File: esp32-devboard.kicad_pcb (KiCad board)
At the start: 2 copper layers, 1 part, among them U1 ESP32-C6-MINI-1/U

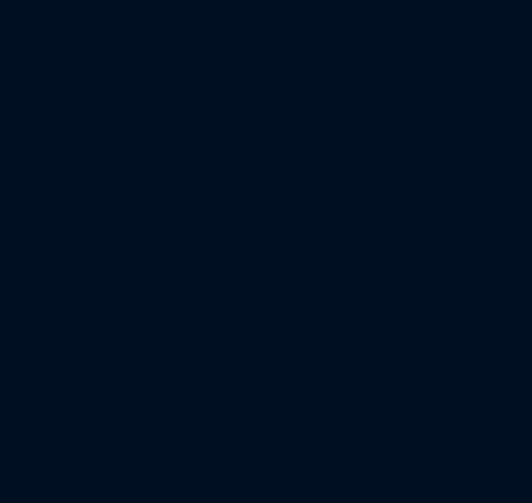
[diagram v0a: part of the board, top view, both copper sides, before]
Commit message: added USB-C connector
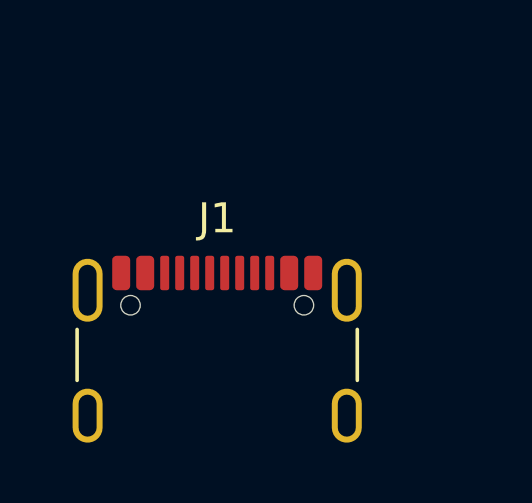
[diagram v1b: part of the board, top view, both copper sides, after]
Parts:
- added J1: USB_C_Receptacle_USB2.0_16P, Connector_USB:USB_C_Receptacle_GCT_USB4105-xx-A_16P_TopMnt_Horizontal, F.Cu at (132.7, 143.9)
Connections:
- net Net-(U1-GND-Pad1) renamed GND
- U1 pad 17: unconnected-(U1-GPIO12/USB_D--Pad17) -> /ESP32/USB_D-
- U1 pad 18: unconnected-(U1-GPIO13/USB_D+-Pad18) -> /ESP32/USB_D+
- U1 pad 3: unconnected-(U1-3V3-Pad3) -> +3.3V
- U1 pad 8: unconnected-(U1-EN/CHIP_PU-Pad8) -> /ESP32/ESP32_EN

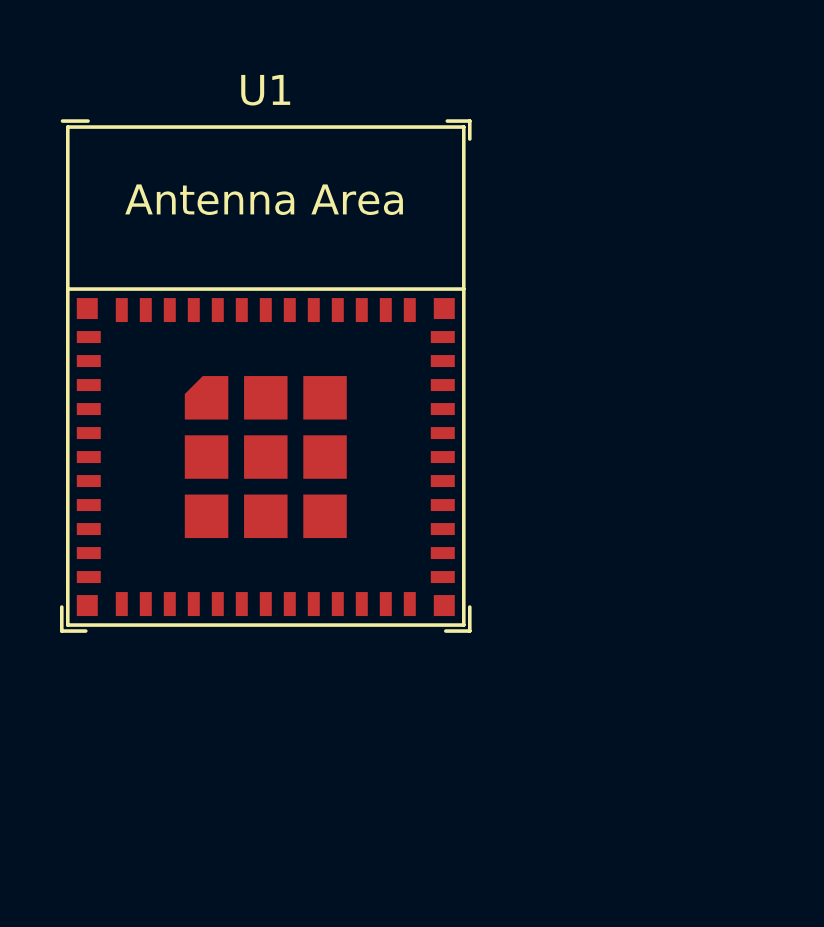
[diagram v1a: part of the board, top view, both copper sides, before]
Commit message: add P/N
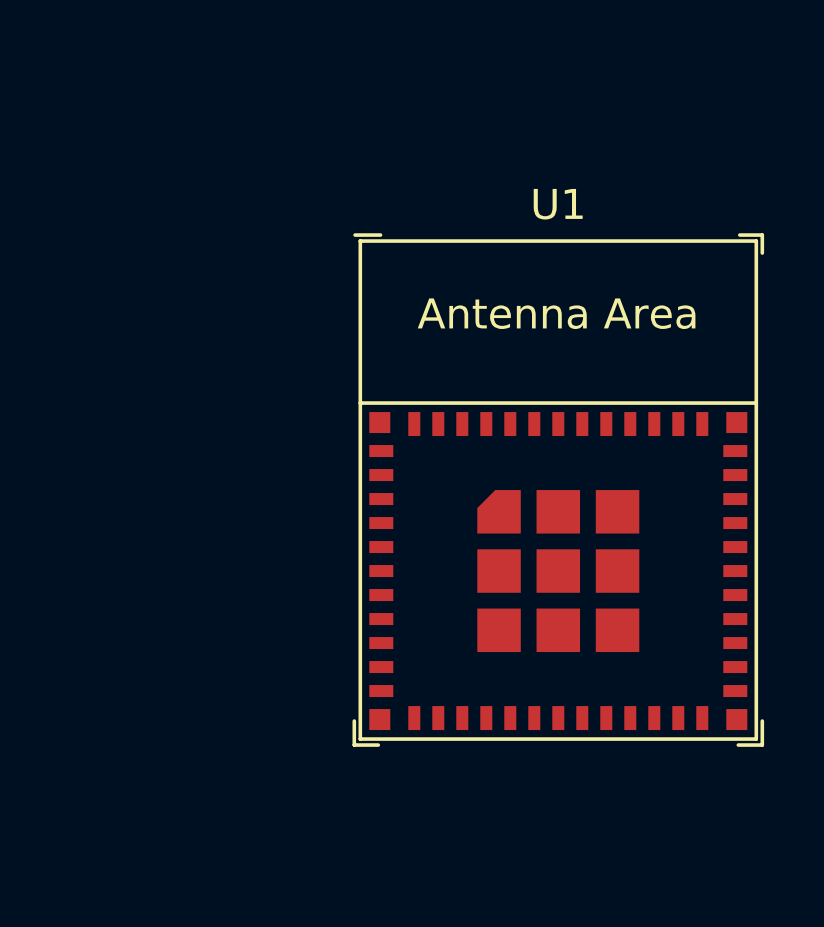
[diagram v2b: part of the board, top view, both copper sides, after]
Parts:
- moved U1 10.5 mm to (144.1, 91.2)
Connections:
- net /ESP32/ESP32_EN renamed /Devices/RST
- net /USB/+5V_USB renamed /USB/VBUSB
- U1 pad 12: unconnected-(U1-GPIO0/ADC1_CH0/XTAL_32K_P-Pad12) -> /ESP32/GPIO_0
- U1 pad 13: unconnected-(U1-GPIO1/ADC1_CH1/XTAL_32K_N-Pad13) -> /ESP32/GPIO_1
- U1 pad 19: unconnected-(U1-GPIO14-Pad19) -> /Devices/FLIP
- U1 pad 20: unconnected-(U1-GPIO15-Pad20) -> /Devices/FLOP
- U1 pad 22: unconnected-(U1-GPIO8-Pad22) -> /ESP32/GPIO_8
- U1 pad 23: unconnected-(U1-GPIO9-Pad23) -> /Devices/BOOT
- U1 pad 24: unconnected-(U1-GPIO18-Pad24) -> /Devices/LED_0
- U1 pad 27: unconnected-(U1-GPIO21-Pad27) -> /ESP32/GPIO_21
- U1 pad 28: unconnected-(U1-GPIO22-Pad28) -> /ESP32/GPIO_22
- U1 pad 29: unconnected-(U1-GPIO23-Pad29) -> /ESP32/GPIO_23
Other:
- copper layers 2 -> 4
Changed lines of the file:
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@@
 	(layers
 		(0 "F.Cu" signal)
+		(1 "In1.Cu" signal)
+		(2 "In2.Cu" signal)
 		(31 "B.Cu" signal)
 		(32 "B.Adhes" user "B.Adhesive")
@@
 	)
 	(setup
+		(stackup
+			(layer "F.SilkS"
+				(type "Top Silk Screen")
+			)
+			(layer "F.Paste"
+				(type "Top Solder Paste")
+			)
+			(layer "F.Mask"
+				(type "Top Solder Mask")
+				(thickness 0.01)
+			)
+			(layer "F.Cu"
+				(type "copper")
+				(thickness 0.035)
+			)
+			(layer "dielectric 1"
+				(type "core")
+				(thickness 0.1)
+				(material "FR4")
+				(epsilon_r 4.5)
+				(loss_tangent 0.02)
+			)
+			(layer "In1.Cu"
+				(type "copper")
+				(thickness 0.035)
+			)
+			(layer "dielectric 2"
+				(type "core")
+				(thickness 1.24)
+				(material "FR4")
+				(epsilon_r 4.5)
+				(loss_tangent 0.02)
+			)
+			(layer "In2.Cu"
+				(type "copper")
+				(thickness 0.035)
+			)
+			(layer "dielectric 3"
+				(type "prepreg")
+				(thickness 0.1)
+				(material "FR4")
+				(epsilon_r 4.5)
+				(loss_tangent 0.02)
+			)
+			(layer "B.Cu"
+				(type "copper")
+				(thickness 0.035)
+			)
+			(layer "B.Mask"
+				(type "Bottom Solder Mask")
+				(thickness 0.01)
+			)
+			(layer "B.Paste"
+				(type "Bottom Solder Paste")
+			)
+			(layer "B.SilkS"
+				(type "Bottom Silk Screen")
+			)
+			(copper_finish "None")
+			(dielectric_constraints no)
+		)
 		(pad_to_mask_clearance 0)
 		(allow_soldermask_bridges_in_footprints no)
@@
 	(net 4 "unconnected-(U1-NC-Pad32)")
 	(net 5 "unconnected-(U1-NC-Pad4)")
-	(net 6 "unconnected-(U1-GPIO1{slash}ADC1_CH1{slash}XTAL_32K_N-Pad13)")
+	(net 6 "/USB/VBUSB")
 	(net 7 "unconnected-(U1-MTDI{slash}GPIO5{slash}ADC1_CH5-Pad10)")
 	(net 8 "unconnected-(U1-U0RXD{slash}GPIO17-Pad30)")
@@
 	(net 11 "unconnected-(U1-MTCK{slash}GPIO6{slash}ADC1_CH6-Pad15)")
 	(net 12 "unconnected-(U1-U0TXD{slash}GPIO16-Pad31)")
-	(net 13 "unconnected-(U1-GPIO18-Pad24)")
+	(net 13 "/ESP32/GPIO_1")
 	(net 14 "unconnected-(U1-MTDO{slash}GPIO7-Pad16)")
-	(net 15 "unconnected-(U1-GPIO8-Pad22)")
+	(net 15 "/Devices/LED_0")
 	(net 16 "unconnected-(U1-NC-Pad35)")
-	(net 17 "unconnected-(U1-GPIO0{slash}ADC1_CH0{slash}XTAL_32K_P-Pad12)")
-	(net 18 "unconnected-(U1-GPIO14-Pad19)")
-	(net 19 "unconnected-(U1-GPIO21-Pad27)")
-	(net 20 "unconnected-(U1-GPIO9-Pad23)")
+	(net 17 "/ESP32/GPIO_8")
+	(net 18 "/ESP32/GPIO_0")
+	(net 19 "/Devices/FLIP")
+	(net 20 "/ESP32/GPIO_21")
 	(net 21 "unconnected-(U1-GPIO19-Pad25)")
 	(net 22 "unconnected-(U1-NC-Pad34)")
 	(net 23 "unconnected-(U1-MTMS{slash}GPIO4{slash}ADC1_CH4-Pad9)")
-	(net 24 "unconnected-(U1-GPIO15-Pad20)")
-	(net 25 "unconnected-(U1-GPIO22-Pad28)")
+	(net 24 "/Devices/BOOT")
+	(net 25 "/Devices/FLOP")
 	(net 26 "unconnected-(U1-NC-Pad33)")
-	(net 27 "unconnected-(U1-GPIO23-Pad29)")
+	(net 27 "/Devices/RST")
 	(net 28 "GND")
 	(net 29 "+3.3V")
-	(net 30 "/ESP32/ESP32_EN")
+	(net 30 "/ESP32/GPIO_22")
 	(net 31 "/ESP32/USB_D-")
 	(net 32 "/ESP32/USB_D+")
 	(net 33 "/USB/CC2")
-	(net 34 "/USB/+5V_USB")
+	(net 34 "/ESP32/GPIO_23")
 	(net 35 "unconnected-(J1-SBU1-PadA8)")
 	(net 36 "/USB/CC1")
@@
 			)
 		)
-		(property "Datasheet" "https://www.usb.org/sites/default/files/documents/usb_type-c.zip"
+		(property "Datasheet" "https://www.mouser.com/datasheet/2/837/usb4215-3472997.pdf"
 			(at 0 0 0)
 			(unlocked yes)
@@
 				(font
 					(size 1.27 1.27)
+					(thickness 0.15)
+				)
+			)
+		)
+		(property "P/N" "640-USB4215-03-A"
+			(at 0 0 0)
+			(unlocked yes)
+			(layer "F.Fab")
+			(hide yes)
+			(effects
+				(font
+					(size 1 1)
 					(thickness 0.15)
 				)
@@
 			(layers "F.Cu" "F.Paste" "F.Mask")
 			(roundrect_rratio 0.25)
-			(net 34 "/USB/+5V_USB")
+			(net 6 "/USB/VBUSB")
 			(pinfunction "VBUS")
 			(pintype "passive")
@@
 			(layers "F.Cu" "F.Paste" "F.Mask")
 			(roundrect_rratio 0.25)
-			(net 34 "/USB/+5V_USB")
+			(net 6 "/USB/VBUSB")
 			(pinfunction "VBUS")
 			(pintype "passive")
@@
 			(layers "F.Cu" "F.Paste" "F.Mask")
 			(roundrect_rratio 0.25)
-			(net 34 "/USB/+5V_USB")
+			(net 6 "/USB/VBUSB")
 			(pinfunction "VBUS")
 			(pintype "passive")
@@
 			(layers "F.Cu" "F.Paste" "F.Mask")
 			(roundrect_rratio 0.25)
-			(net 34 "/USB/+5V_USB")
+			(net 6 "/USB/VBUSB")
 			(pinfunction "VBUS")
 			(pintype "passive")
@@
 	(footprint "PCM_Espressif:ESP32-C6-MINI-1"
 		(layer "F.Cu")
-		(at 134.3 87.35)
+		(at 144.05 91.15)
 		(descr "ESP32-C6-MINI-1: https://www.espressif.com/sites/default/files/documentation/esp32-c6-mini-1_datasheet_en.pdf")
 		(tags "ESP32-C6")
@@
 			(net 10 "unconnected-(U1-GPIO2{slash}ADC1_CH2-Pad5)")
 			(pinfunction "GPIO2/ADC1_CH2")
-			(pintype "bidirectional")
+			(pintype "bidirectional+no_connect")
 		)
 		(pad "6" smd rect
@@
 			(net 1 "unconnected-(U1-GPIO3{slash}ADC1_CH3-Pad6)")
 			(pinfunction "GPIO3/ADC1_CH3")
-			(pintype "bidirectional")
+			(pintype "bidirectional+no_connect")
 		)
 		(pad "7" smd rect
@@
 			(size 0.4 0.8)
 			(layers "F.Cu" "F.Paste" "F.Mask")
-			(net 30 "/ESP32/ESP32_EN")
+			(net 27 "/Devices/RST")
 			(pinfunction "EN/CHIP_PU")
 			(pintype "input")
@@
 			(net 23 "unconnected-(U1-MTMS{slash}GPIO4{slash}ADC1_CH4-Pad9)")
 			(pinfunction "MTMS/GPIO4/ADC1_CH4")
-			(pintype "bidirectional")
+			(pintype "bidirectional+no_connect")
 		)
 		(pad "10" smd rect
@@
 			(net 7 "unconnected-(U1-MTDI{slash}GPIO5{slash}ADC1_CH5-Pad10)")
 			(pinfunction "MTDI/GPIO5/ADC1_CH5")
-			(pintype "bidirectional")
+			(pintype "bidirectional+no_connect")
 		)
 		(pad "11" smd rect
@@
 			(size 0.4 0.8)
 			(layers "F.Cu" "F.Paste" "F.Mask")
-			(net 17 "unconnected-(U1-GPIO0{slash}ADC1_CH0{slash}XTAL_32K_P-Pad12)")
+			(net 18 "/ESP32/GPIO_0")
 			(pinfunction "GPIO0/ADC1_CH0/XTAL_32K_P")
 			(pintype "bidirectional")
@@
 			(size 0.4 0.8)
 			(layers "F.Cu" "F.Paste" "F.Mask")
-			(net 6 "unconnected-(U1-GPIO1{slash}ADC1_CH1{slash}XTAL_32K_N-Pad13)")
+			(net 13 "/ESP32/GPIO_1")
 			(pinfunction "GPIO1/ADC1_CH1/XTAL_32K_N")
 			(pintype "bidirectional")
@@
 			(net 11 "unconnected-(U1-MTCK{slash}GPIO6{slash}ADC1_CH6-Pad15)")
 			(pinfunction "MTCK/GPIO6/ADC1_CH6")
-			(pintype "bidirectional")
+			(pintype "bidirectional+no_connect")
 		)
 		(pad "16" smd rect
@@
 			(net 14 "unconnected-(U1-MTDO{slash}GPIO7-Pad16)")
 			(pinfunction "MTDO/GPIO7")
-			(pintype "bidirectional")
+			(pintype "bidirectional+no_connect")
 		)
 		(pad "17" smd rect
@@
 			(size 0.4 0.8)
 			(layers "F.Cu" "F.Paste" "F.Mask")
-			(net 18 "unconnected-(U1-GPIO14-Pad19)")
+			(net 19 "/Devices/FLIP")
 			(pinfunction "GPIO14")
 			(pintype "bidirectional")
@@
 			(size 0.4 0.8)
 			(layers "F.Cu" "F.Paste" "F.Mask")
-			(net 24 "unconnected-(U1-GPIO15-Pad20)")
+			(net 25 "/Devices/FLOP")
 			(pinfunction "GPIO15")
 			(pintype "bidirectional")
@@
 			(size 0.4 0.8)
 			(layers "F.Cu" "F.Paste" "F.Mask")
-			(net 15 "unconnected-(U1-GPIO8-Pad22)")
+			(net 17 "/ESP32/GPIO_8")
 			(pinfunction "GPIO8")
 			(pintype "bidirectional")
@@
 			(size 0.4 0.8)
 			(layers "F.Cu" "F.Paste" "F.Mask")
-			(net 20 "unconnected-(U1-GPIO9-Pad23)")
+			(net 24 "/Devices/BOOT")
 			(pinfunction "GPIO9")
 			(pintype "bidirectional")
@@
 			(size 0.4 0.8)
 			(layers "F.Cu" "F.Paste" "F.Mask")
-			(net 13 "unconnected-(U1-GPIO18-Pad24)")
+			(net 15 "/Devices/LED_0")
 			(pinfunction "GPIO18")
 			(pintype "bidirectional")
@@
 			(net 21 "unconnected-(U1-GPIO19-Pad25)")
 			(pinfunction "GPIO19")
-			(pintype "bidirectional")
+			(pintype "bidirectional+no_connect")
 		)
 		(pad "26" smd rect
@@
 			(net 9 "unconnected-(U1-GPIO20-Pad26)")
 			(pinfunction "GPIO20")
-			(pintype "bidirectional")
+			(pintype "bidirectional+no_connect")
 		)
 		(pad "27" smd rect
@@
 			(size 0.4 0.8)
 			(layers "F.Cu" "F.Paste" "F.Mask")
-			(net 19 "unconnected-(U1-GPIO21-Pad27)")
+			(net 20 "/ESP32/GPIO_21")
 			(pinfunction "GPIO21")
 			(pintype "bidirectional")
@@
 			(size 0.4 0.8)
 			(layers "F.Cu" "F.Paste" "F.Mask")
-			(net 25 "unconnected-(U1-GPIO22-Pad28)")
+			(net 30 "/ESP32/GPIO_22")
 			(pinfunction "GPIO22")
 			(pintype "bidirectional")
@@
 			(size 0.4 0.8)
 			(layers "F.Cu" "F.Paste" "F.Mask")
-			(net 27 "unconnected-(U1-GPIO23-Pad29)")
+			(net 34 "/ESP32/GPIO_23")
 			(pinfunction "GPIO23")
 			(pintype "bidirectional")
@@
 			(net 8 "unconnected-(U1-U0RXD{slash}GPIO17-Pad30)")
 			(pinfunction "U0RXD/GPIO17")
-			(pintype "bidirectional")
+			(pintype "bidirectional+no_connect")
 		)
 		(pad "31" smd rect
@@
 			(net 12 "unconnected-(U1-U0TXD{slash}GPIO16-Pad31)")
 			(pinfunction "U0TXD/GPIO16")
-			(pintype "bidirectional")
+			(pintype "bidirectional+no_connect")
 		)
 		(pad "32" smd rect
@@
 			(polygon
 				(pts
-					(xy 140.9 84.45) (xy 127.7 84.45) (xy 127.7 79.05) (xy 140.9 79.05)
+					(xy 150.65 88.25) (xy 137.45 88.25) (xy 137.45 82.85) (xy 150.65 82.85)
 				)
 			)
@@
 		(polygon
 			(pts
-				(xy 112.7 84.45) (xy 112.7 64.05) (xy 155.9 64.05) (xy 155.9 84.45)
-			)
-		)
+				(xy 122.45 88.25) (xy 122.45 67.85) (xy 165.65 67.85) (xy 165.65 88.25)
+			)
+		)
+	)
+	(group ""
+		(members "9e491c97-c408-47aa-a825-656574b5255b" "efe0206d-e05d-4263-8e52-4d6ee51e22c0")
 	)
 )

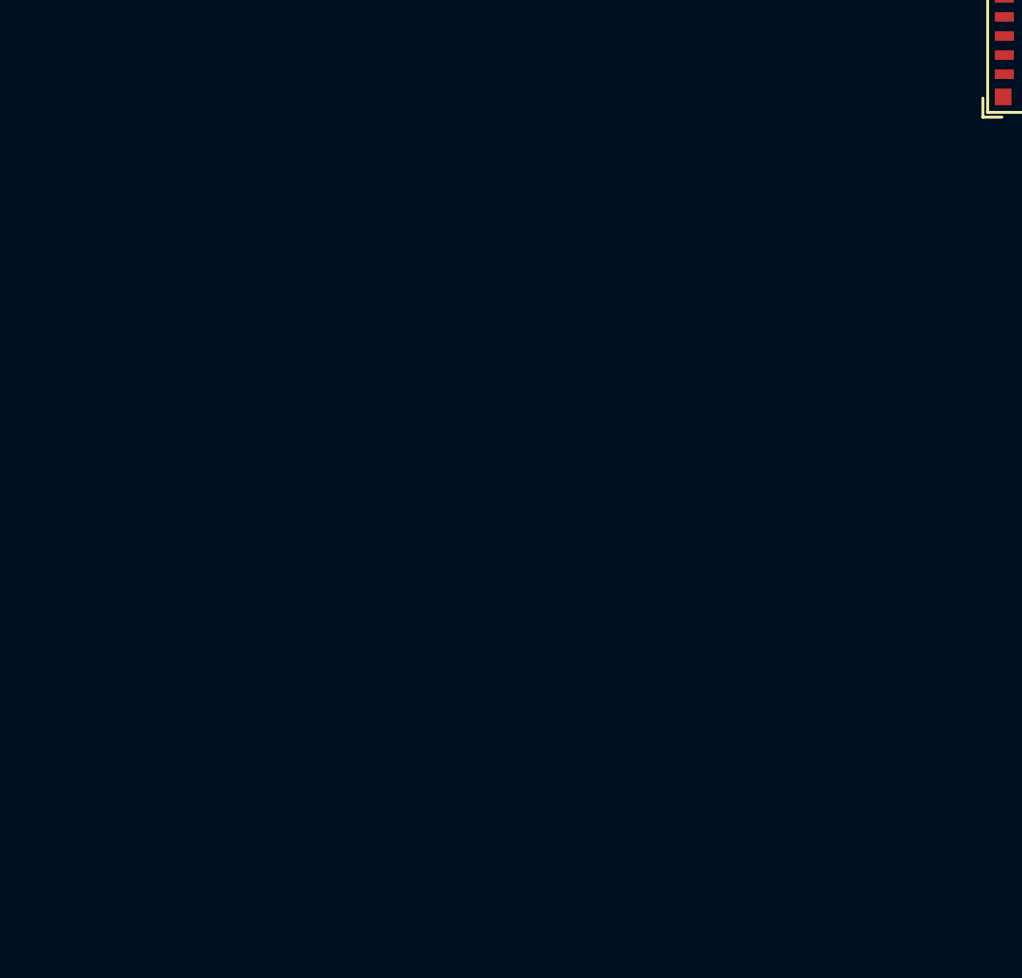
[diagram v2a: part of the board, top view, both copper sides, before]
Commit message: add testpoints
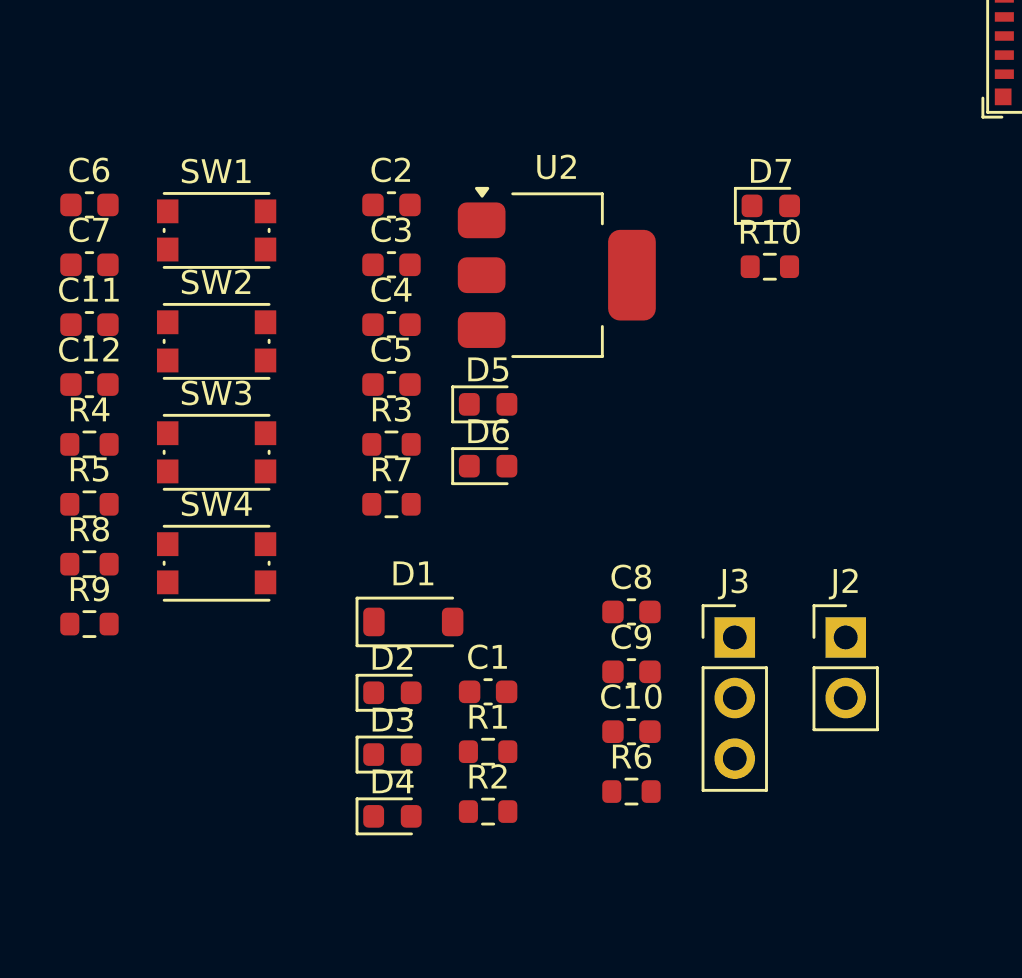
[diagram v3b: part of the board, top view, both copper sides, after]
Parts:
- added C1: 10u, Capacitor_SMD:C_0603_1608Metric, F.Cu at (116.5, 123.7)
- added C10: 0.1u, Capacitor_SMD:C_0603_1608Metric, F.Cu at (122.5, 125.4)
- added C11: 0.1u, Capacitor_SMD:C_0603_1608Metric, F.Cu at (99.8, 108.3)
- added C12: 0.1u, Capacitor_SMD:C_0603_1608Metric, F.Cu at (99.8, 110.9)
- added C2: 10u, Capacitor_SMD:C_0603_1608Metric, F.Cu at (112.5, 103.3)
- added C3: 0.1u, Capacitor_SMD:C_0603_1608Metric, F.Cu at (112.5, 105.8)
- added C4: 10u, Capacitor_SMD:C_0603_1608Metric, F.Cu at (112.5, 108.3)
- added C5: 0.1u, Capacitor_SMD:C_0603_1608Metric, F.Cu at (112.5, 110.9)
- added C6: 0.1u, Capacitor_SMD:C_0603_1608Metric, F.Cu at (99.8, 103.3)
- added C7: 0.1u, Capacitor_SMD:C_0603_1608Metric, F.Cu at (99.8, 105.8)
- added C8: 1u, Capacitor_SMD:C_0603_1608Metric, F.Cu at (122.5, 120.4)
- added C9: 10u, Capacitor_SMD:C_0603_1608Metric, F.Cu at (122.5, 122.9)
- added D1: 1N5819HW-7-F, Diode_SMD:D_SOD-123, F.Cu at (113.4, 120.8)
- added D2: TVS, Diode_SMD:D_0603_1608Metric, F.Cu at (112.5, 123.8)
- added D3: TVS, Diode_SMD:D_0603_1608Metric, F.Cu at (112.5, 126.4)
- added D4: TVS, Diode_SMD:D_0603_1608Metric, F.Cu at (112.5, 129.0)
- added D5: PWR, LED_SMD:LED_0603_1608Metric, F.Cu at (116.5, 111.7)
- added D6: PWR, LED_SMD:LED_0603_1608Metric, F.Cu at (116.5, 114.3)
- added D7: DANGER, LED_SMD:LED_0603_1608Metric, F.Cu at (128.4, 103.4)
- added J2: CA, Connector_PinHeader_2.54mm:PinHeader_1x02_P2.54mm_Vertical, F.Cu at (131.5, 121.5)
- added J3: CB, Connector_PinHeader_2.54mm:PinHeader_1x03_P2.54mm_Vertical, F.Cu at (126.8, 121.5)
- added R1: 5.1k, Resistor_SMD:R_0603_1608Metric, F.Cu at (116.5, 126.2)
- added R10: 47, Resistor_SMD:R_0603_1608Metric, F.Cu at (128.3, 105.9)
- added R2: 5.1k, Resistor_SMD:R_0603_1608Metric, F.Cu at (116.5, 128.8)
- added R3: 47, Resistor_SMD:R_0603_1608Metric, F.Cu at (112.5, 113.4)
- added R4: 10k, Resistor_SMD:R_0603_1608Metric, F.Cu at (99.8, 113.4)
- added R5: 10k, Resistor_SMD:R_0603_1608Metric, F.Cu at (99.8, 115.9)
- added R6: 3.3k, Resistor_SMD:R_0603_1608Metric, F.Cu at (122.5, 127.9)
- added R7: 47, Resistor_SMD:R_0603_1608Metric, F.Cu at (112.5, 115.9)
- added R8: 10k, Resistor_SMD:R_0603_1608Metric, F.Cu at (99.8, 118.4)
- added R9: 10k, Resistor_SMD:R_0603_1608Metric, F.Cu at (99.8, 120.9)
- added SW1: BOOT, Button_Switch_SMD:SW_Push_1P1T_NO_CK_KMR2, F.Cu at (105.1, 104.4)
- added SW2: RST, Button_Switch_SMD:SW_Push_1P1T_NO_CK_KMR2, F.Cu at (105.1, 109.0)
- added SW3: FLIP, Button_Switch_SMD:SW_Push_1P1T_NO_CK_KMR2, F.Cu at (105.1, 113.7)
- added SW4: FLOP, Button_Switch_SMD:SW_Push_1P1T_NO_CK_KMR2, F.Cu at (105.1, 118.3)
- added U2: AMS1117-3.3, Package_TO_SOT_SMD:SOT-223-3_TabPin2, F.Cu at (119.4, 106.3)
